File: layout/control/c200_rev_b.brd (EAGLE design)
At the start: 200 x 50 mm, 81 parts, among them IC1 STM32F103C8T, IC2 LP2985-SOT23-5, IC3 IC_USBLC6-2, IC4 IC_USBLC6-2, IC5 LT1619ES8, IC6 LP2985-SOT23-5, IC7 IRF7470, SW1 2P2T, T1 LPISR, Y1 532-CRYSTAL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

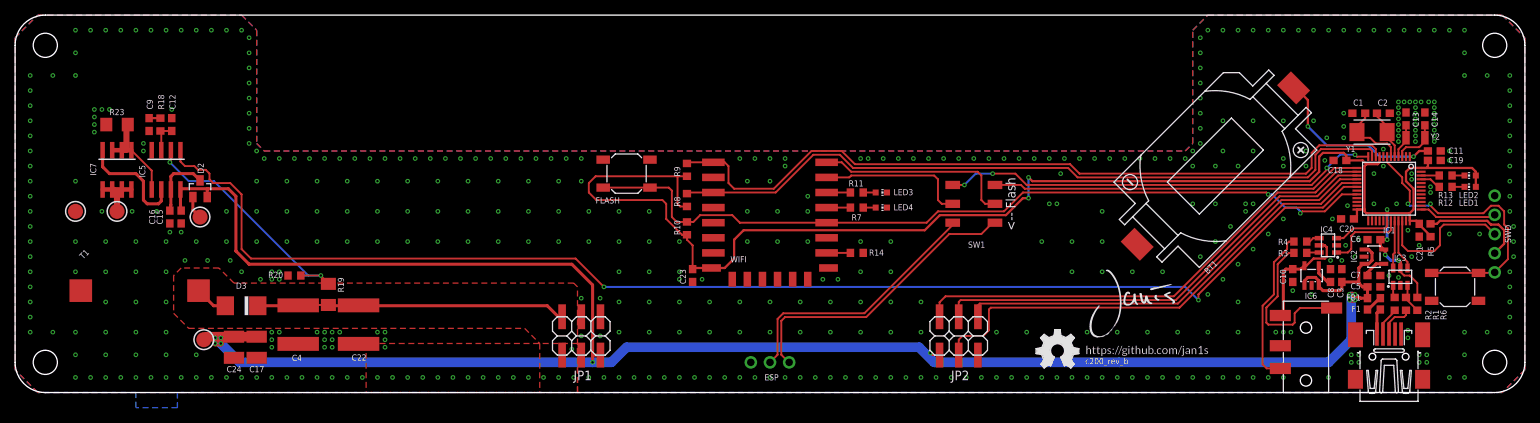
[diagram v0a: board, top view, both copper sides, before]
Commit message: Added HV module
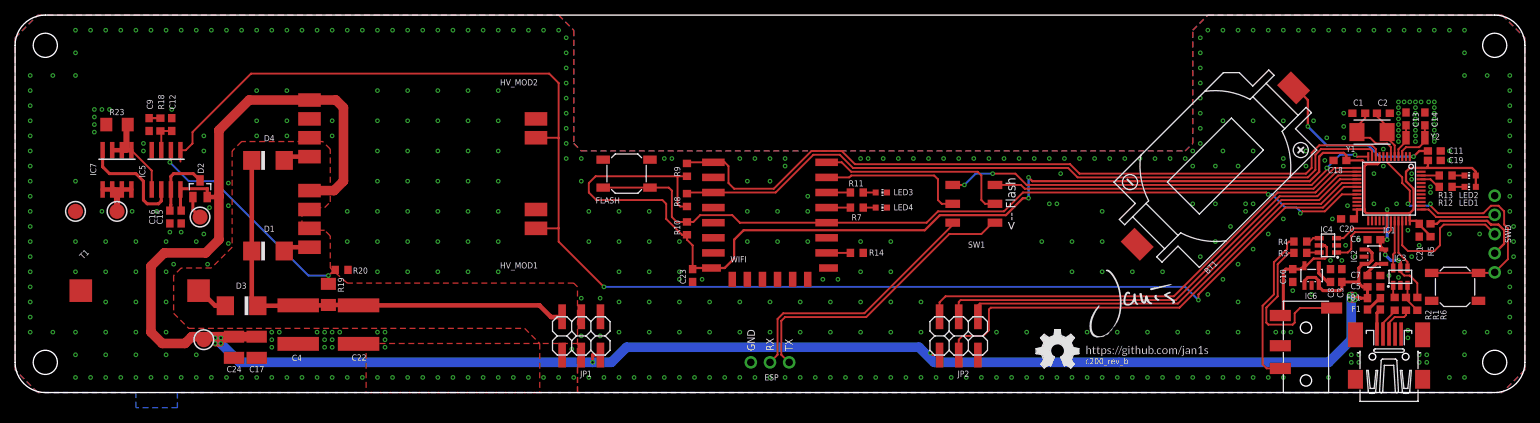
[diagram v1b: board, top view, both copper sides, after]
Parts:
- added D1, D4: ES2, diode:DO-214AA
- added HV_MOD1, HV_MOD2: HV5W, hv-mod:HV5W-D
- moved R20 6.29 mm to (43.2, 16.2), turned to 0 degrees
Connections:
- new net N$40: D1.A, HV_MOD1.HV
- new net N$41: D4.A, HV_MOD2.HV
- net +5V: now also HV_MOD1.+5V, HV_MOD2.+5V
- net GND: now also HV_MOD1.GND1, HV_MOD1.GND2, HV_MOD1.GND3, HV_MOD2.GND1, HV_MOD2.GND2, HV_MOD2.GND3
- net HV: now also D1.C, D4.C
- net HV_EN: now also HV_MOD1.EN, HV_MOD2.EN
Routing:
- net HV_EN: track 176.3 -> 199.8 mm
- net HV: track 42.9 -> 60.6 mm
- net +5V: track 300.7 -> 308.2 mm
- net N$41: track 0.00 -> 3.66 mm
- net N$40: track 0.00 -> 3.66 mm
- net N$17: track 32.9 -> 31.1 mm
